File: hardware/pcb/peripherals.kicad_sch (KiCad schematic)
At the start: 11 parts, among them J401 Speaker, U401 PCF8563T, U402 MAX98357A, Y401 32.768kHz

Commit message: Use power symbols for the CM0 3.3V and 1.8V rails
Rename CM0_3V3 to +3V3_CM0 and CM0_1V8 to +1V8_CM0, replace their
labels on the cm0, display and peripherals sheets with power symbols,
and update the docs to match.

Co-Authored-By: Claude Opus 5.5 <noreply@anthropic.com>
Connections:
- net CM0_3V3 renamed +3V3_CM0
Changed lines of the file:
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@@
-		)
-	)
-	(global_label "CM0_3V3"
-		(shape passive)
-		(at 170.18 95.25 90)
-		(fields_autoplaced yes)
-		(effects
-			(font
-				(size 1.27 1.27)
-			)
-			(justify left)
-		)
-		(property "Intersheetrefs" "${INTERSHEET_REFS}"
-			(at 170.18 95.25 0)
-			(hide yes)
-			(show_name no)
-			(do_not_autoplace no)
-			(effects
-				(font
-					(size 1.27 1.27)
-				)
-			)
 		)
 	)
@@
 					(unit 1)
 				)
+			)
+		)
+	)
+	(symbol
+		(lib_id "power:+3V3")
+		(at 170.18 95.25 0)
+		(unit 1)
+		(exclude_from_sim no)
+		(in_bom yes)
+		(on_board yes)
+		(dnp no)
+		(property "Reference" "#PWR185"
+			(at 170.18 95.25 0)
+			(hide yes)
+			(effects
+				(font
+					(size 1.27 1.27)
+				)
+			)
+		)
+		(property "Value" "+3V3_CM0"
+			(at 170.18 91.44 0)
+			(effects
+				(font
+					(size 1.27 1.27)
+				)
+			)
+		)
+		(property "Footprint" ""
+			(at 170.18 95.25 0)
+			(hide yes)
+			(effects
+				(font
+					(size 1.27 1.27)
+				)
+			)
+		)
+		(property "Datasheet" ""
+			(at 170.18 95.25 0)
+			(hide yes)
+			(effects
+				(font
+					(size 1.27 1.27)
+				)
+			)
+		)
+		(pin "1"
+		)
+		(instances
+			(project "skjar"
+				(path "/1040ccb5-ae9e-4b0f-85c7-cf44771f813b/eb07638f-cc27-4cc3-b503-1b87189697b4"
+					(reference "#PWR185")
+					(unit 1)
+				)

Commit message: Assign 0603 parts, use 30k for ILM, and switch the LDO to AP2127
Give every resistor and capacitor a 0603 footprint and an LCSC number
(Basic where possible), change the ILM resistor to a 30k Basic part,
and replace the XC6206 with an AP2127N-3.3 from stock. Record the
decisions and drop the resolved open items.

Co-Authored-By: Claude Opus 5.5 <noreply@anthropic.com>
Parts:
- C401, C403: footprint (none) -> Capacitor_SMD:C_0603_1608Metric; LCSC (none) -> C14663
- C402: footprint (none) -> Capacitor_SMD:C_0603_1608Metric; LCSC (none) -> C96446
- R401: footprint (none) -> Resistor_SMD:R_0603_1608Metric; LCSC (none) -> C25804
- R402: footprint (none) -> Resistor_SMD:R_0603_1608Metric; LCSC (none) -> C22961
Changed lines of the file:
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@@
 			)
 		)
-		(property "Footprint" ""
+		(property "Footprint" "Capacitor_SMD:C_0603_1608Metric"
 			(at 321.0052 74.93 0)
 			(hide yes)
 			(show_name no)
 			(do_not_autoplace no)
+			(effects
+				(font
+					(size 1.27 1.27)
+				)
+			)
+		)
+		(property "LCSC" "C14663"
+			(at 320.04 71.12 0)
+			(show_name no)
+			(do_not_autoplace no)
+			(hide yes)
 			(effects
 				(font
@@
 			)
 		)
-		(property "Footprint" ""
+		(property "Footprint" "Capacitor_SMD:C_0603_1608Metric"
 			(at 160.9852 69.85 0)
 			(hide yes)
 			(show_name no)
 			(do_not_autoplace no)
+			(effects
+				(font
+					(size 1.27 1.27)
+				)
+			)
+		)
+		(property "LCSC" "C14663"
+			(at 160.02 66.04 0)
+			(show_name no)
+			(do_not_autoplace no)
+			(hide yes)
 			(effects
 				(font
@@
 			)
 		)
-		(property "Footprint" ""
+		(property "Footprint" "Resistor_SMD:R_0603_1608Metric"
 			(at 168.402 99.06 0)
 			(hide yes)
 			(show_name no)
 			(do_not_autoplace no)
+			(effects
+				(font
+					(size 1.27 1.27)
+				)
+			)
+		)
+		(property "LCSC" "C25804"
+			(at 170.18 99.06 0)
+			(show_name no)
+			(do_not_autoplace no)
+			(hide yes)
 			(effects
 				(font
@@
 			)
 		)
-		(property "Footprint" ""
+		(property "Footprint" "Capacitor_SMD:C_0603_1608Metric"
 			(at 310.8452 74.93 0)
 			(hide yes)
 			(show_name no)
 			(do_not_autoplace no)
+			(effects
+				(font
+					(size 1.27 1.27)
+				)
+			)
+		)
+		(property "LCSC" "C96446"
+			(at 309.88 71.12 0)
+			(show_name no)
+			(do_not_autoplace no)
+			(hide yes)
 			(effects
 				(font
@@
 			)
 		)
-		(property "Footprint" ""
+		(property "Footprint" "Resistor_SMD:R_0603_1608Metric"
 			(at 239.522 124.46 0)
 			(hide yes)
@@
 			(effects
 				(font
+					(size 1.27 1.27)
+				)
+			)
+		)
+		(property "LCSC" "C22961"
+			(at 241.3 124.46 0)
+			(show_name no)
+			(do_not_autoplace no)
+			(hide yes)
+			(effects
+				(font

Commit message: Switch the RTC crystal to a 9 pF part from stock
Use the JGHC S3132768092070 (C479190, 9 pF load) for Y401 instead of
the 12.5 pF Epson FC-135, since the PCF8563 is characterized with an
8 pF crystal. Same 3215 outline; assign the 3215 footprint.

Co-Authored-By: Claude Opus 5.5 <noreply@anthropic.com>
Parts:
- Y401: footprint (none) -> Crystal:Crystal_SMD_3215-2Pin_3.2x1.5mm; LCSC C32346 -> C479190
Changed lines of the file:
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@@
 			)
 		)
-		(property "Footprint" ""
+		(property "Footprint" "Crystal:Crystal_SMD_3215-2Pin_3.2x1.5mm"
 			(at 93.98 88.9 0)
 			(hide yes)
@@
 			)
 		)
-		(property "LCSC" "C32346"
+		(property "LCSC" "C479190"
 			(at 93.98 88.9 0)
 			(hide yes)

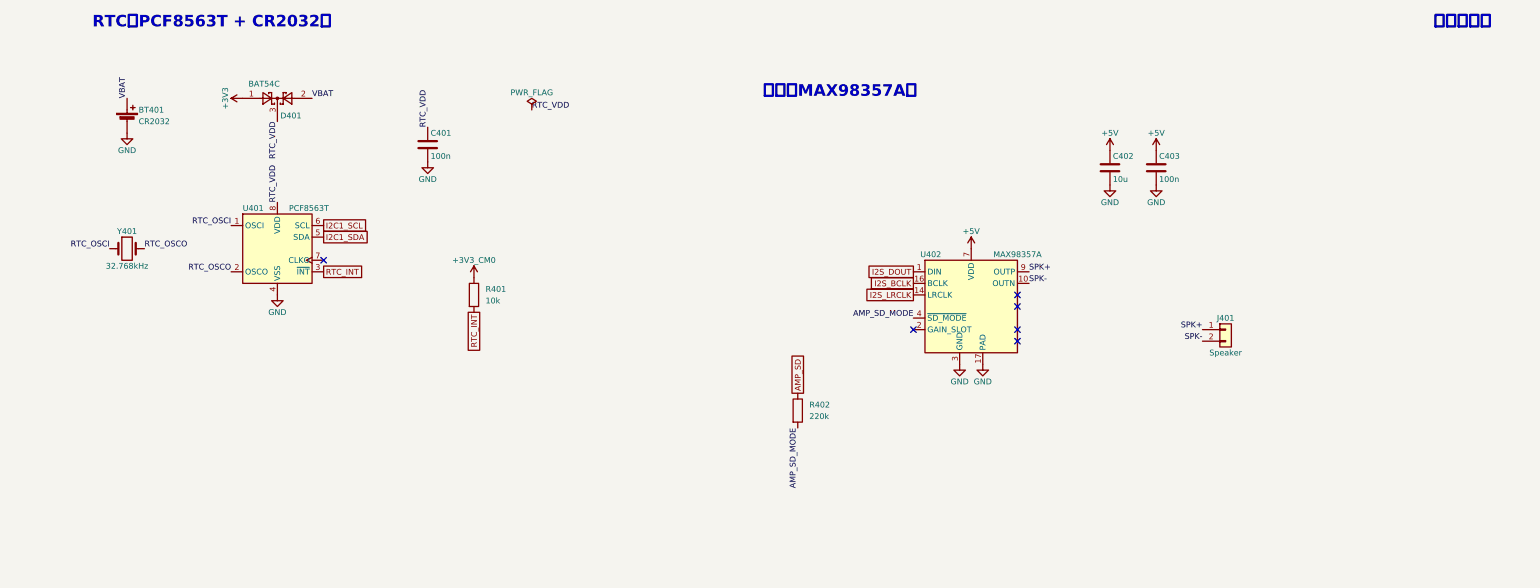
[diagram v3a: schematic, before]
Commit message: Add audio, microSD and keyboard I2C, and place parts on the PCB
Schematics:
- Swap the MAX98357A for the TLV320DAC3100 (headphone and speaker out).
  A 12 MHz oscillator drives MCLK and the codec is the I2S clock master,
  so the stock simple-audio-card works without a custom machine driver.
- Add the microSD slot for the CM0Lite; the SD pull-ups are footprints only.
- Add HID over I2C from the RP2040 to the CM0 (KB_SDA/KB_SCL/KB_INT) on
  i2c-gpio, so the keyboard works on stock Raspberry Pi OS. Add test pads.
- Use power symbols for +1V1, assign footprints and LCSC numbers, and
  fix global label shapes.

PCB: 228.6 x 146.2 mm outline and a provisional bottom-side placement,
with HID USB top-left and Linux USB top-right. Add footprints for the CM0,
TPS2121 (RUX), the 22-pin DSI FPC and the CR2032 holder.

Docs: record the decisions and open items. Add a draft device tree
overlay for the audio codec.

Co-Authored-By: Claude Opus 5.5 <noreply@anthropic.com>
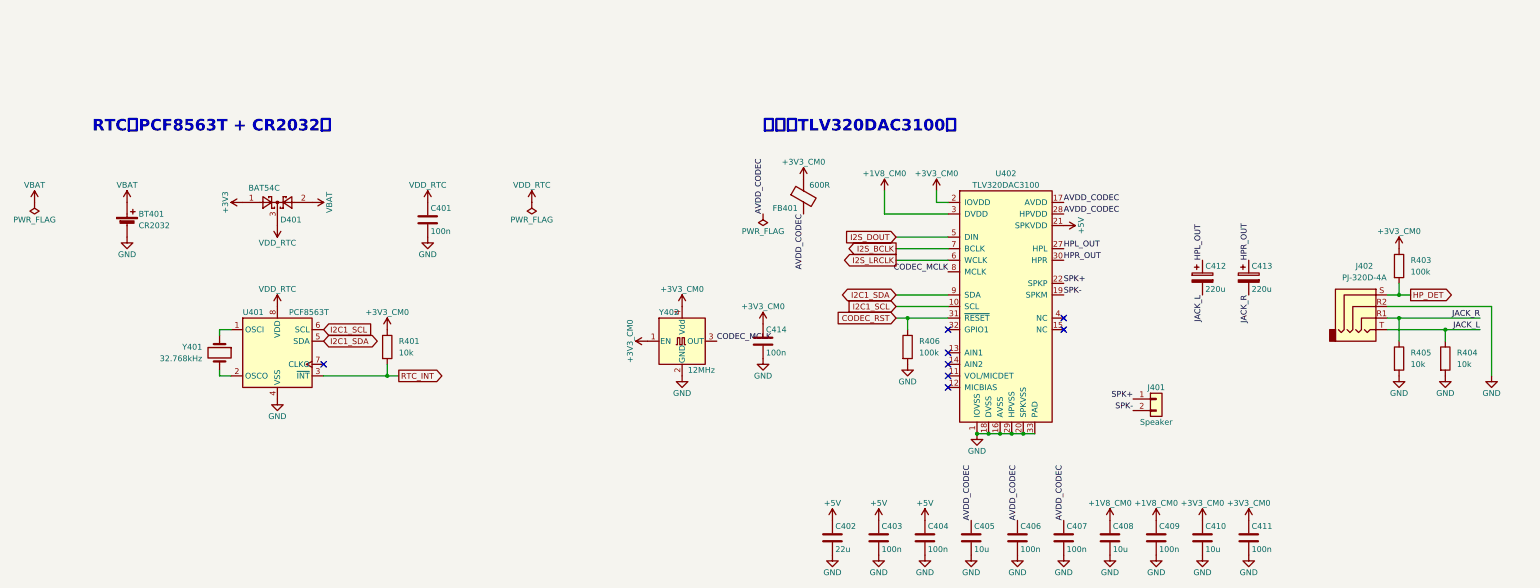
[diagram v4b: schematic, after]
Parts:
- removed R402: 220k, Resistor_SMD:R_0603_1608Metric, symbol Device:R
- removed U402: MAX98357A, Package_DFN_QFN:TQFN-16-1EP_3x3mm_P0.5mm_EP1.23x1.23mm, symbol Audio:MAX98357A
- added C404, C406, C407, C409, C411, C414: 100n, Capacitor_SMD:C_0603_1608Metric, symbol Device:C
- added C405, C408, C410: 10u, Capacitor_SMD:C_0603_1608Metric, symbol Device:C
- added C412, C413: 220u, Capacitor_SMD:CP_Elec_6.3x7.7, symbol Device:C_Polarized
- added FB401: 600R, Inductor_SMD:L_0805_2012Metric, symbol Device:FerriteBead
- added J402: PJ-320D-4A, Connector_Audio:Jack_3.5mm_KoreanHropartsElec_PJ-320D-4A_Horizontal, symbol Connector_Audio:AudioJack4
- added R403, R406: 100k, Resistor_SMD:R_0603_1608Metric, symbol Device:R
- added R404, R405: 10k, Resistor_SMD:R_0603_1608Metric, symbol Device:R
- added U402: TLV320DAC3100, Package_DFN_QFN:Texas_RHB0032E_VQFN-32-1EP_5x5mm_P0.5mm_EP3.45x3.45mm, symbol Skjar:TLV320DAC3100
- added Y402: 12MHz, Oscillator:Oscillator_SMD_Abracon_ASE-4Pin_3.2x2.5mm, symbol Oscillator:ASE-xxxMHz
- BT401: footprint (none) -> Skjar:BatteryHolder_MYOUNG_MY-2032-08
- C402: value 10u -> 22u; footprint Capacitor_SMD:C_0603_1608Metric -> Capacitor_SMD:C_0805_2012Metric; LCSC C96446 -> C45783
- J401: footprint (none) -> Connector_Molex:Molex_PicoBlade_53261-0271_1x02-1MP_P1.25mm_Horizontal; LCSC (none) -> C177225
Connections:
- net +3V3_CM0: now also C410.1, C411.1, C414.1, FB401.1, R403.1, U402.2 (IOVDD), Y402.1 (EN), Y402.4 (Vdd)
- net +5V: now also C404.1, U402.21 (SPKVDD), U402.24 (SPKVDD)
- net GND: now also C404.2, C405.2, C406.2, C407.2, C408.2, C409.2, C410.2, C411.2, C414.2, J402.R2, R404.2, R405.2, R406.2, U402.1 (IOVSS), U402.16 (AVSS), U402.18 (DVSS), U402.20 (SPKVSS), U402.25 (SPKVSS), U402.29 (HPVSS), U402.33 (PAD), Y402.2 (GND)
- net I2C1_SCL: now also U402.10 (SCL)
- net I2C1_SDA: now also U402.9 (SDA)
- net I2S_BCLK: now also U402.7 (BCLK)
- net I2S_DOUT: now also U402.5 (DIN)
- net I2S_LRCLK: now also U402.6 (WCLK)
- net SPK+: now also U402.22 (SPKP), U402.26 (SPKP)
- net SPK-: now also U402.19 (SPKM), U402.23 (SPKM)
- net RTC_OSCI: no longer names the net of U401.1 (OSCI), Y401.1
- net RTC_OSCO: no longer names the net of U401.2 (OSCO), Y401.2
- net RTC_VDD renamed VDD_RTC
- new net +1V8_CM0: C408.1, C409.1, U402.3 (DVDD)
- new net AVDD_CODEC: C405.1, C406.1, C407.1, FB401.2, U402.17 (AVDD), U402.28 (HPVDD)
- new net CODEC_MCLK: U402.8 (MCLK), Y402.3 (OUT)
- new net CODEC_RST: R406.1, U402.31 (~{RESET})
- new net HPL_OUT: C412.1, U402.27 (HPL)
- new net HPR_OUT: C413.1, U402.30 (HPR)
- new net HP_DET: J402.S, R403.2
- new net JACK_L: C412.2, J402.T, R404.1
- new net JACK_R: C413.2, J402.R1, R405.1
- no-connect marks 6 -> 8
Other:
- note added: "音声（TLV320DAC3100）"
- note removed: "シート外へ"
- note removed: "音声（MAX98357A）"
- moved on the sheet: BT401, C401, D401, R401, U401, Y401

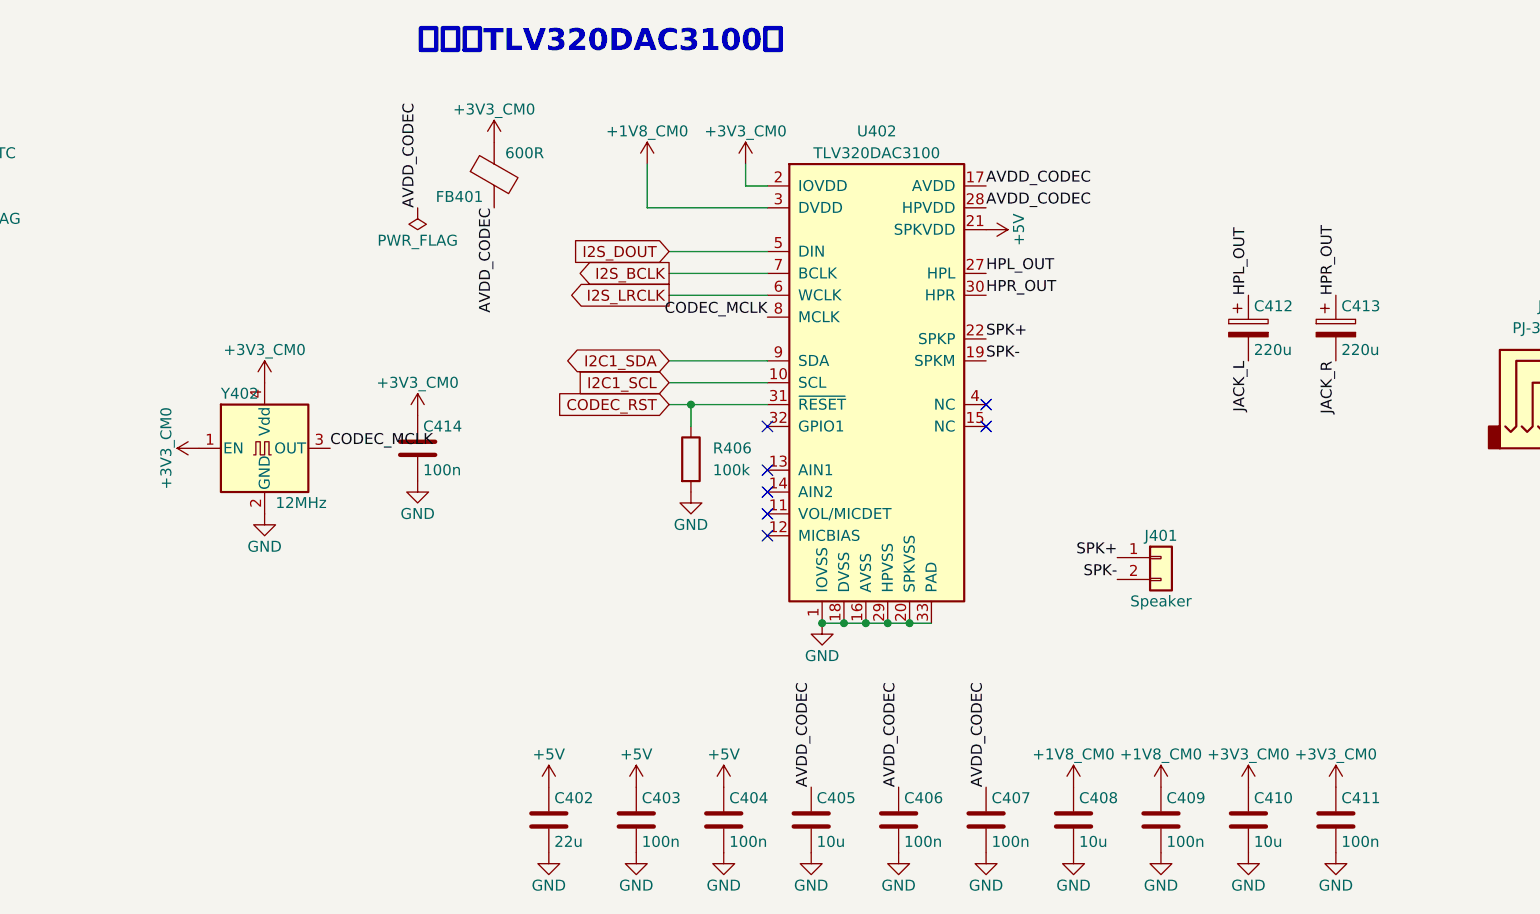
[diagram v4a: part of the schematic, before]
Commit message: Add per-key RGB, finish schematic wiring, and document HID over I2C
- Add SK6812MINI-E per-key RGB with a switched +5V_LED rail and an
  AHCT buffer on the data line; remove SW102 to free GPIO20
- Use D_Small for the matrix diodes and replace labels with wires
- Tidy the keymatrix sheet layout without changing connectivity
- Document the HID over I2C keyboard path, back-power rules and
  role split across README and docs

Co-Authored-By: Claude Opus 5.5 <noreply@anthropic.com>
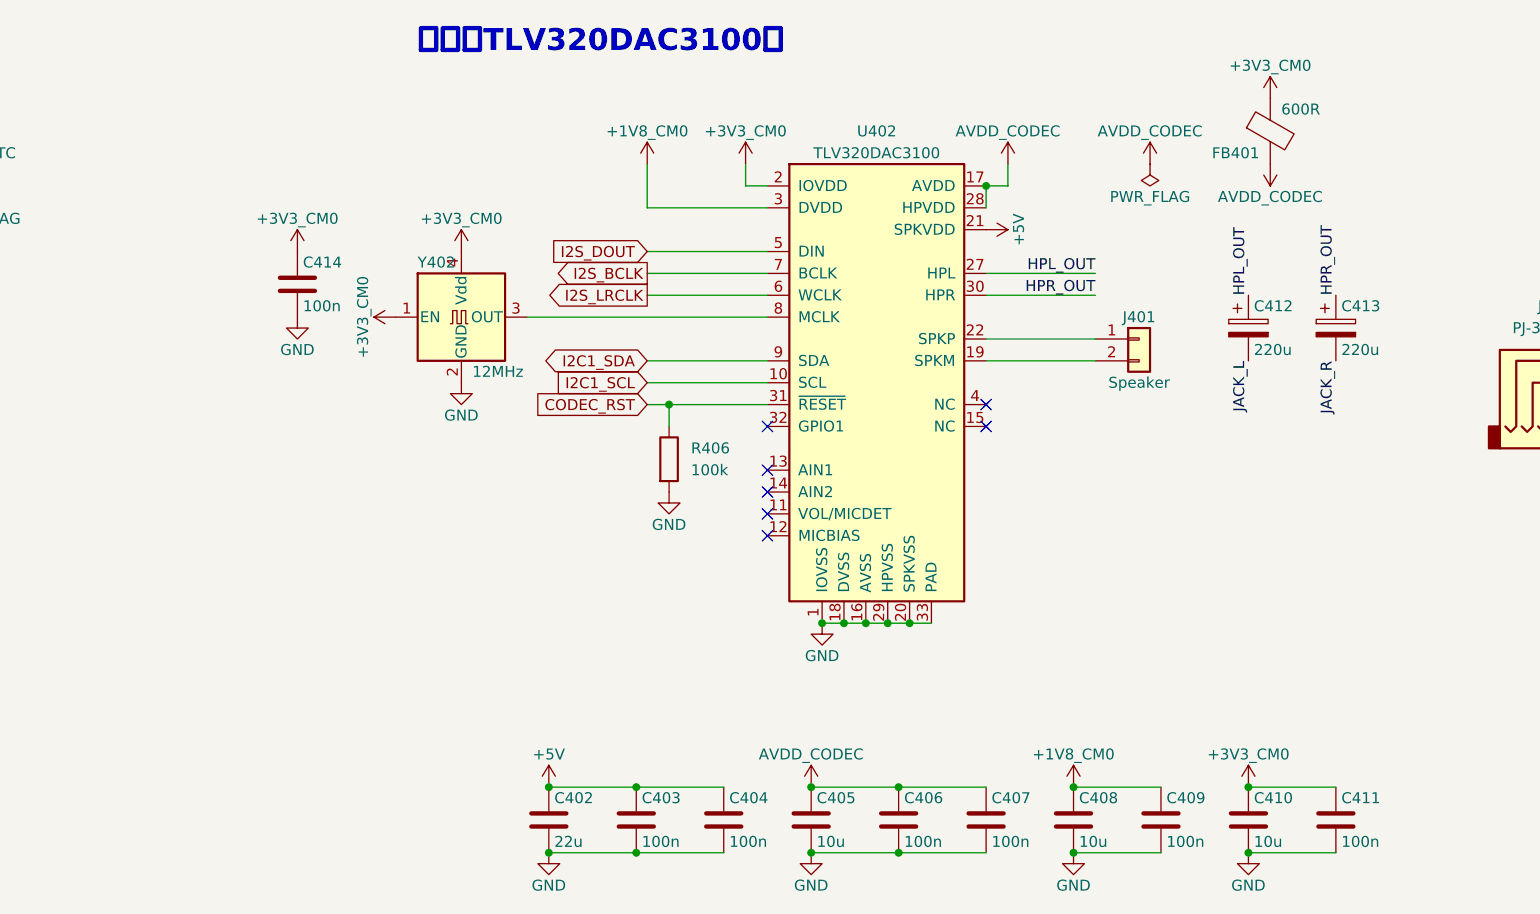
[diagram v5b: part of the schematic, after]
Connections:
- net CODEC_MCLK: no longer names the net of U402.8 (MCLK), Y402.3 (OUT)
- net SPK+: no longer names the net of J401.1 (Pin_1), U402.22 (SPKP), U402.26 (SPKP)
- net SPK-: no longer names the net of J401.2 (Pin_2), U402.19 (SPKM), U402.23 (SPKM)
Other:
- moved on the sheet: C414, FB401, J401, R406, Y402
